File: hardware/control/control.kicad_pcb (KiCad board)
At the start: 2 copper layers, 47 x 26 mm, 46 parts, among them J1 Conn_01x02_Pin, J2 USB_C_Receptacle, J3 Conn_01x02_Pin, J5 Conn_01x02_Pin, Q1 2N7002, SW1 KMS221GLFS, SW2 KMS221GLFS, SW3 KMS221GLFS, SW4 KMS221GLFS, U1 ESP32-C6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

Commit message: done routing
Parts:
- removed C15, C16: 1u, Capacitor_SMD:C_0603_1608Metric
- removed C30: 22u, Capacitor_SMD:C_1206_3216Metric
- removed C5, C6, C7: 100n, Capacitor_SMD:C_0603_1608Metric
- removed L6: 22u, Inductor_SMD:L_Wuerth_MAPI-4030
- removed U4: STI3508, Package_TO_SOT_SMD:SOT-23-6
- removed U7: NCP163AFCT330T2G, Package_CSP:WLCSP-4_0.64x0.64mm_Layout2x2_P0.35mm
- added L4: 22u, Inductor_SMD:L_Wuerth_MAPI-4030, F.Cu at (123.0, 114.4)
- added Q2: 2N7002, Package_TO_SOT_SMD:SOT-23, F.Cu at (122.6, 118.4)
- added R13: 1, Resistor_SMD:R_0603_1608Metric, F.Cu at (122.2, 111.3)
- added R15: 1, Resistor_SMD:R_0603_1608Metric, F.Cu at (119.9, 118.4)
- added R36: 100, Resistor_SMD:R_0603_1608Metric, F.Cu at (132.9, 116.0)
- added U3: W25Q128JVP, Package_SON:WSON-8-1EP_6x5mm_P1.27mm_EP3.4x4.3mm, F.Cu at (106.3, 108.5)
- R12: value 47k -> 10k
- moved R10 19.0 mm to (106.5, 101.6)
- moved D7 16.0 mm to (140.2, 118.2), turned to 0 degrees
- moved R12 15.7 mm to (108.1, 101.6), turned to -90 degrees
- moved C31 13.5 mm to (128.0, 108.0)
- moved BT2 12.7 mm to (145.4, 117.6)
- moved J3 12.2 mm to (132.3, 118.4), turned to -90 degrees
- moved R32 11.2 mm to (129.1, 118.4), turned to -90 degrees
- moved R9 8.63 mm to (133.5, 106.8), turned to 0 degrees
- moved R11 7.92 mm to (131.1, 107.7), turned to -90 degrees
- moved R35 6.83 mm to (114.9, 118.3), turned to 90 degrees
- moved Q1 6.27 mm to (135.0, 117.8), turned to 90 degrees
- moved R31 5.99 mm to (102.1, 106.0), turned to 180 degrees
- moved R34 5.73 mm to (118.3, 108.3), turned to 0 degrees
- moved U5 5.16 mm to (137.9, 110.1), turned to 180 degrees
- moved R33 4.14 mm to (115.1, 108.3), turned to 0 degrees
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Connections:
- BT2 pad 1: /power/V_bat -> Net-(BT2-+)
- C31 pad 1: /power/V_bat -> /+5V
- D7 pad 1: /valves1/24V -> /+5V
- D7 pad 2: Net-(D7-A) -> Net-(BT2-+)
- J3 pad 1: /+3V3 -> Net-(J3-Pin_1)
- J5 pad 2: /valves1/24V -> Net-(J5-Pin_2)
- L3 pad 1: /power/V_bat -> /+5V
- R10 pad 1: /valves1/0V6 -> Net-(J2-CC2)
- R12 pad 1: /valves1/0V6 -> /GND
- R12 pad 2: /valves1/24V -> Net-(J2-CC1)
- SW3 pad 2: /power/V_bat -> /+5V
- U5 pad 5: /power/V_bat -> /+5V
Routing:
- net /GND: track 0.00 -> 54.8 mm, vias 0 -> 14
- net /controller/pwm2: track 0.00 -> 50.0 mm, vias 0 -> 4
- net /+5V: track 0.00 -> 49.0 mm, vias 0 -> 5
- net /controller/pwm1: track 0.00 -> 47.7 mm, vias 0 -> 4
- net /controller/enable: track 0.00 -> 37.1 mm, vias 0 -> 4
- net Net-(U1-GPIO20/SDIO_DATA0/FSPICS4): track 0.00 -> 35.3 mm, vias 0 -> 2
- net /+3V3: track 0.00 -> 31.1 mm, vias 0 -> 14
- net /controller/boot: track 0.00 -> 27.1 mm, vias 0 -> 2
- net /controller/led_on: track 0.00 -> 24.7 mm, vias 0 -> 2
- net /controller/reset: track 0.00 -> 22.9 mm, vias 0 -> 4
- net Net-(U1-SPIWP/GPIO26): track 0.00 -> 12.9 mm, vias 0 -> 2
- net Net-(U1-SPIQ/GPIO25): track 0.00 -> 12.3 mm, vias 0 -> 2
- net Net-(U1-GPIO12/USB_D-): track 0.00 -> 12.2 mm, vias 0 -> 2
- net Net-(U1-SPICS0/GPIO24): track 0.00 -> 11.8 mm, vias 0 -> 2
- net Net-(U1-SPID/GPIO30): track 0.00 -> 10.3 mm, vias 0 -> 2
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- added copper zone on In1.Cu, net /+3V3
- added copper zone on B.Cu, net /GND
- added copper zone on F.Cu, net /GND
- added copper zone on In2.Cu, net /GND
- added copper zone on F.Cu, net /controller/antenna
- added copper zone on In1.Cu, net /controller/antenna
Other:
- copper layers 2 -> 4

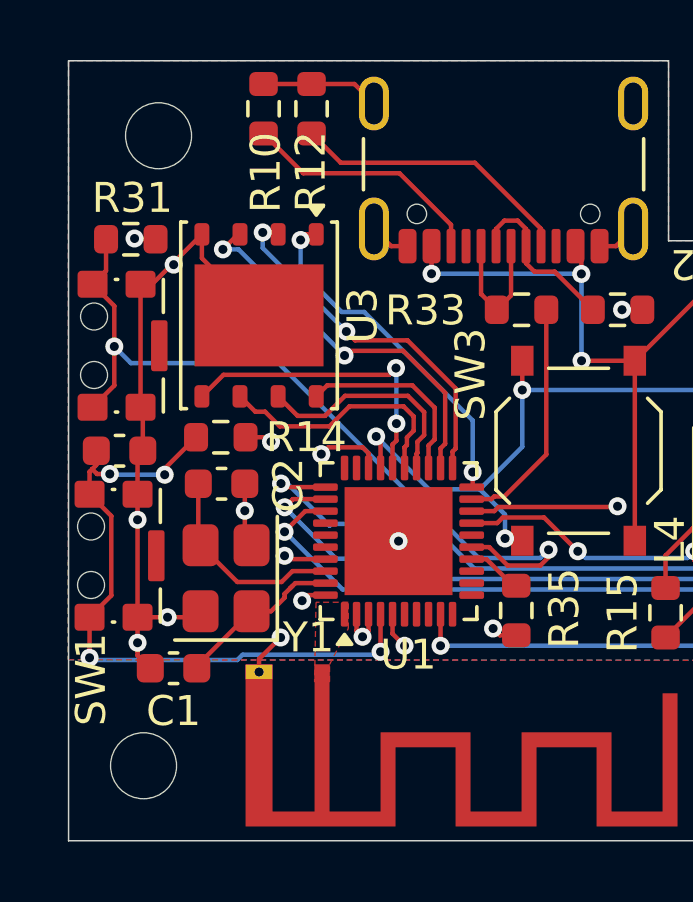
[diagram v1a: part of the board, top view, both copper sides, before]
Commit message: changed switches due to shortage
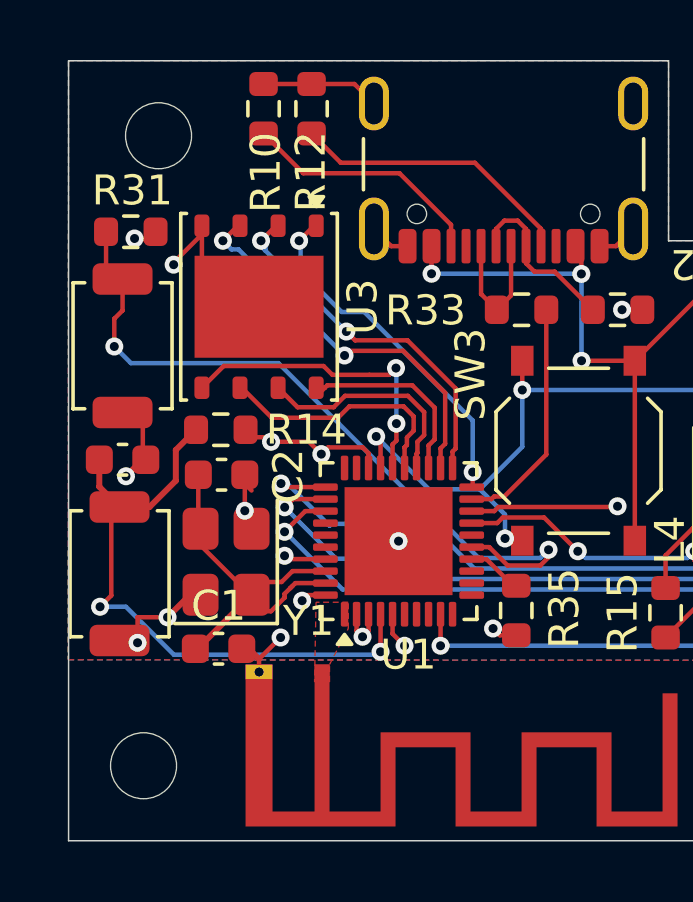
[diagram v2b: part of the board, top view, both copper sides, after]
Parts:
- removed SW1: KMS221GLFS, Button_Switch_SMD:SW_SPST_CK_KMS2xxGP
- added SW5: KMS221GLFS, Button_Switch_SMD:SW_SPST_TS-1088-xR020, F.Cu at (101.7, 117.1)
- SW2: footprint Button_Switch_SMD:SW_SPST_CK_KMS2xxGP -> Button_Switch_SMD:SW_SPST_TS-1088-xR020
- moved C1 1.63 mm to (105.0, 119.6), turned to 0 degrees
- moved Y1 0.55 mm to (105.2, 116.7)
- moved C20 0.32 mm to (101.8, 113.3)
- moved C2 0.30 mm to (105.1, 113.8)
- moved U3 0.29 mm to (106.3, 108.2)
- moved R14 0.25 mm to (105.1, 112.3)
- moved R31 0.25 mm to (102.1, 105.7)
- moved SW2 0.20 mm to (101.8, 109.5), turned to 90 degrees
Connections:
- Q2 pad 1: /controller/jet_on -> /valves1/pwm
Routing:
- net /GND: track 54.8 -> 45.2 mm
- net /controller/boot: track 27.1 -> 24.1 mm
- net /controller/reset: track 22.9 -> 20.6 mm, vias 4 -> 2
- net /+3V3: track 31.1 -> 32.9 mm
